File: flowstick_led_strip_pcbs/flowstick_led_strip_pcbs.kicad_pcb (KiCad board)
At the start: 2 copper layers, 8.6 x 127.4 mm, 92 parts, among them J1 LED, J2 LED

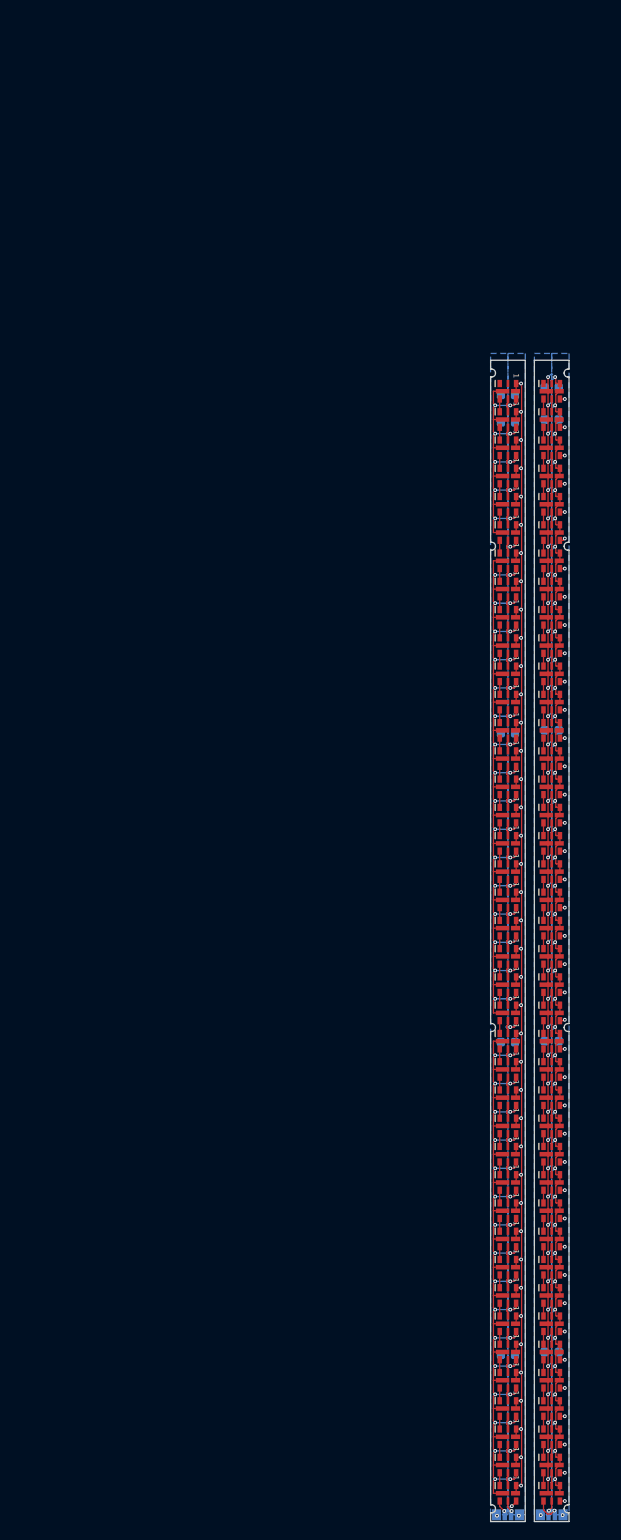
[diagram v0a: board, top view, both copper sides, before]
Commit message: work on rev2 + panelize LED strips
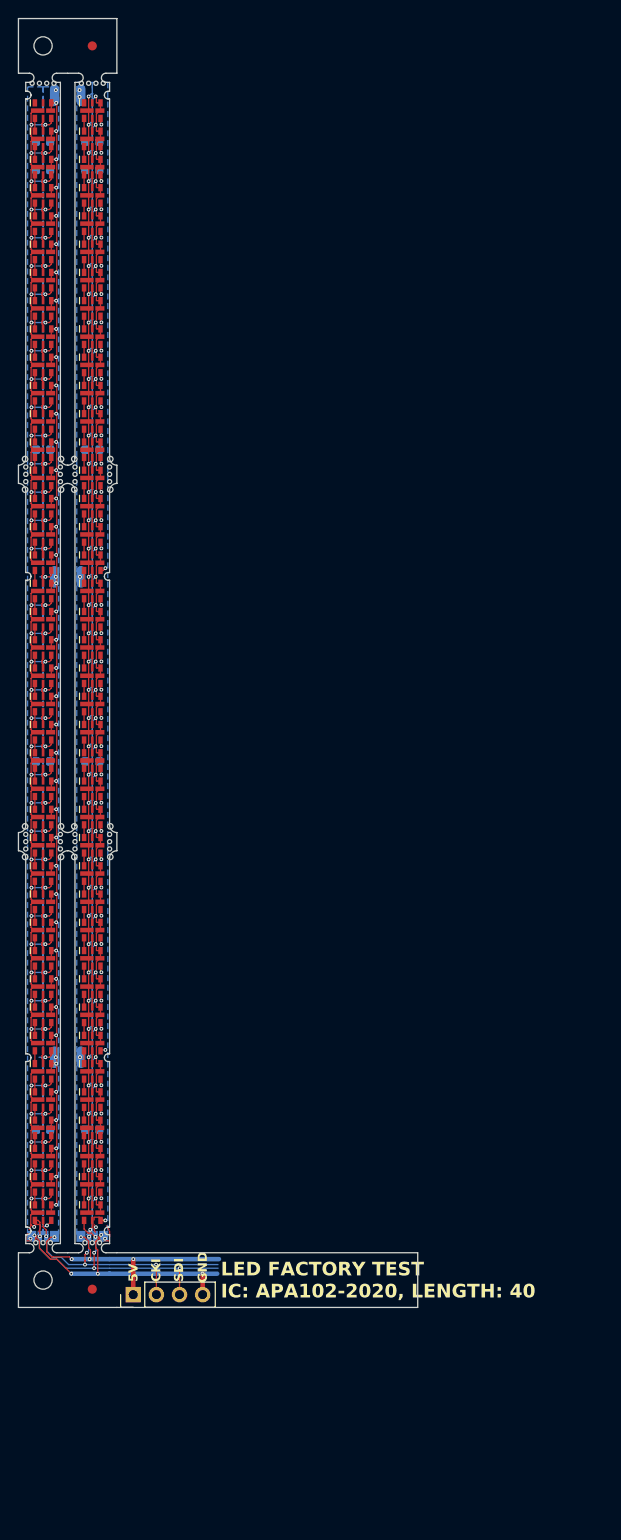
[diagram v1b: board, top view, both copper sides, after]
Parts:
- added H1: MountingHole_Pad, custom:single_b2b_pad_doublewide, B.Cu at (52.1, 136.5)
- added H2: MountingHole_Pad, custom:single_b2b_pad_doublewide, B.Cu at (55.0, 136.5)
- added H3: MountingHole_Pad, custom:single_b2b_pad_doublewide, B.Cu at (52.1, 83.8)
- added H4: MountingHole_Pad, custom:single_b2b_pad_doublewide, B.Cu at (55.0, 83.8)
- added H5: MountingHole_Pad, custom:single_b2b_pad_doublewide, B.Cu at (52.1, 30.9)
- added H6: MountingHole_Pad, custom:single_b2b_pad_doublewide, B.Cu at (55.0, 30.9)
- added J3: FACTORY_TEST, Connector_PinHeader_2.54mm:PinHeader_1x04_P2.54mm_Vertical, F.Cu at (60.8, 162.5)
- added REF**: mousebite_mini4, custom:mousebite_mini4, F.Cu at (50.9, 29.6)
- added REF**: mousebite_5, custom:mousebite_5, F.Cu at (49.0, 72.5)
- added REF**: Fiducial_1mm_Mask2mm, Fiducial:Fiducial_1mm_Mask2mm, F.Cu at (56.3, 161.9)
- added REF**: mousebite_mini3, custom:mousebite_mini3, F.Cu at (50.9, 156.8)
- added REF**: mousebite_5, custom:mousebite_5, F.Cu at (58.2, 112.8)
- added REF**: MountingHole_2mm, MountingHole:MountingHole_2mm, F.Cu at (50.9, 160.9)
- added REF**: mousebite_5, custom:mousebite_5, F.Cu at (52.8, 112.8)
- added REF**: mousebite_mini4, custom:mousebite_mini4, F.Cu at (56.3, 29.6)
- added REF**: mousebite_5, custom:mousebite_5, F.Cu at (54.4, 112.8)
- added REF**: mousebite_5, custom:mousebite_5, F.Cu at (58.2, 72.5)
- added REF**: mousebite_5, custom:mousebite_5, F.Cu at (54.4, 72.5)
- added REF**: MountingHole_2mm, MountingHole:MountingHole_2mm, F.Cu at (50.9, 25.5)
- added REF**: mousebite_5, custom:mousebite_5, F.Cu at (52.8, 72.5)
- added REF**: mousebite_mini3, custom:mousebite_mini3, F.Cu at (56.3, 156.8)
- added REF**: mousebite_5, custom:mousebite_5, F.Cu at (49.0, 112.8)
- added REF**: Fiducial_1mm_Mask2mm, Fiducial:Fiducial_1mm_Mask2mm, F.Cu at (56.3, 25.5)
- moved C3 59.7 mm to (50.9, 69.8)
- moved D1 59.6 mm to (50.9, 153.5)
- moved D6 59.6 mm to (50.9, 138.0)
- moved C2 59.6 mm to (50.9, 104.0)
- moved D10 59.6 mm to (50.9, 125.6)
- moved D11 59.6 mm to (50.9, 122.5)
- moved D12 59.6 mm to (50.9, 119.4)
- moved D14 59.6 mm to (50.9, 113.2)
- moved D15 59.6 mm to (50.9, 110.1)
- moved D16 59.6 mm to (50.9, 107.0)
- moved D17 59.6 mm to (50.9, 103.9)
- moved D18 59.6 mm to (50.9, 100.8)
- moved D19 59.6 mm to (50.9, 97.7)
- moved D2 59.6 mm to (50.9, 150.4)
- moved D20 59.6 mm to (50.9, 94.6)
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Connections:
- C10 pad 1: /strip_r/+5V -> /strip_l/+5V
- C10 pad 2: /strip_r/GND -> /strip_l/GND
- C6 pad 1: /strip_r/+5V -> /strip_l/+5V
- C6 pad 2: /strip_r/GND -> /strip_l/GND
- C7 pad 1: /strip_r/+5V -> /strip_l/+5V
- C7 pad 2: /strip_r/GND -> /strip_l/GND
- C8 pad 1: /strip_r/+5V -> /strip_l/+5V
- C8 pad 2: /strip_r/GND -> /strip_l/GND
- C9 pad 1: /strip_r/+5V -> /strip_l/+5V
- C9 pad 2: /strip_r/GND -> /strip_l/GND
- D41 pad 1: /strip_r/+5V -> /strip_l/+5V
- D41 pad 4: /strip_r/SDI -> /strip_l/SDI
- D41 pad 5: /strip_r/CKI -> /strip_l/CKI
- D41 pad 6: /strip_r/GND -> /strip_l/GND
- D42 pad 1: /strip_r/+5V -> /strip_l/+5V
- D42 pad 6: /strip_r/GND -> /strip_l/GND
- D43 pad 1: /strip_r/+5V -> /strip_l/+5V
- D43 pad 6: /strip_r/GND -> /strip_l/GND
- D44 pad 1: /strip_r/+5V -> /strip_l/+5V
- D44 pad 6: /strip_r/GND -> /strip_l/GND
- D45 pad 1: /strip_r/+5V -> /strip_l/+5V
- D45 pad 6: /strip_r/GND -> /strip_l/GND
- D46 pad 1: /strip_r/+5V -> /strip_l/+5V
- D46 pad 6: /strip_r/GND -> /strip_l/GND
- D47 pad 1: /strip_r/+5V -> /strip_l/+5V
- D47 pad 6: /strip_r/GND -> /strip_l/GND
- D48 pad 1: /strip_r/+5V -> /strip_l/+5V
- D48 pad 6: /strip_r/GND -> /strip_l/GND
- D49 pad 1: /strip_r/+5V -> /strip_l/+5V
- D49 pad 6: /strip_r/GND -> /strip_l/GND
- D50 pad 1: /strip_r/+5V -> /strip_l/+5V
- D50 pad 6: /strip_r/GND -> /strip_l/GND
- D51 pad 1: /strip_r/+5V -> /strip_l/+5V
- D51 pad 6: /strip_r/GND -> /strip_l/GND
- D52 pad 1: /strip_r/+5V -> /strip_l/+5V
- D52 pad 6: /strip_r/GND -> /strip_l/GND
- D53 pad 1: /strip_r/+5V -> /strip_l/+5V
- D53 pad 6: /strip_r/GND -> /strip_l/GND
- D54 pad 1: /strip_r/+5V -> /strip_l/+5V
- D54 pad 6: /strip_r/GND -> /strip_l/GND
- D55 pad 1: /strip_r/+5V -> /strip_l/+5V
- D55 pad 6: /strip_r/GND -> /strip_l/GND
- D56 pad 1: /strip_r/+5V -> /strip_l/+5V
- D56 pad 6: /strip_r/GND -> /strip_l/GND
- D57 pad 1: /strip_r/+5V -> /strip_l/+5V
- D57 pad 6: /strip_r/GND -> /strip_l/GND
- D58 pad 1: /strip_r/+5V -> /strip_l/+5V
- D58 pad 6: /strip_r/GND -> /strip_l/GND
- D59 pad 1: /strip_r/+5V -> /strip_l/+5V
- D59 pad 6: /strip_r/GND -> /strip_l/GND
- D60 pad 1: /strip_r/+5V -> /strip_l/+5V
- D60 pad 6: /strip_r/GND -> /strip_l/GND
- D61 pad 1: /strip_r/+5V -> /strip_l/+5V
- D61 pad 6: /strip_r/GND -> /strip_l/GND
- D62 pad 1: /strip_r/+5V -> /strip_l/+5V
- D62 pad 6: /strip_r/GND -> /strip_l/GND
- D63 pad 1: /strip_r/+5V -> /strip_l/+5V
- D63 pad 6: /strip_r/GND -> /strip_l/GND
- D64 pad 1: /strip_r/+5V -> /strip_l/+5V
- D64 pad 6: /strip_r/GND -> /strip_l/GND
- D65 pad 1: /strip_r/+5V -> /strip_l/+5V
- D65 pad 6: /strip_r/GND -> /strip_l/GND
- D66 pad 1: /strip_r/+5V -> /strip_l/+5V
- D66 pad 6: /strip_r/GND -> /strip_l/GND
- D67 pad 1: /strip_r/+5V -> /strip_l/+5V
- D67 pad 6: /strip_r/GND -> /strip_l/GND
- D68 pad 1: /strip_r/+5V -> /strip_l/+5V
- D68 pad 6: /strip_r/GND -> /strip_l/GND
- D69 pad 1: /strip_r/+5V -> /strip_l/+5V
- D69 pad 6: /strip_r/GND -> /strip_l/GND
- D70 pad 1: /strip_r/+5V -> /strip_l/+5V
- D70 pad 6: /strip_r/GND -> /strip_l/GND
- D71 pad 1: /strip_r/+5V -> /strip_l/+5V
- D71 pad 6: /strip_r/GND -> /strip_l/GND
- D72 pad 1: /strip_r/+5V -> /strip_l/+5V
- D72 pad 6: /strip_r/GND -> /strip_l/GND
- D73 pad 1: /strip_r/+5V -> /strip_l/+5V
- D73 pad 6: /strip_r/GND -> /strip_l/GND
- D74 pad 1: /strip_r/+5V -> /strip_l/+5V
- D74 pad 6: /strip_r/GND -> /strip_l/GND
- D75 pad 1: /strip_r/+5V -> /strip_l/+5V
- D75 pad 6: /strip_r/GND -> /strip_l/GND
- D76 pad 1: /strip_r/+5V -> /strip_l/+5V
- D76 pad 6: /strip_r/GND -> /strip_l/GND
- D77 pad 1: /strip_r/+5V -> /strip_l/+5V
- D77 pad 6: /strip_r/GND -> /strip_l/GND
- D78 pad 1: /strip_r/+5V -> /strip_l/+5V
- D78 pad 6: /strip_r/GND -> /strip_l/GND
- D79 pad 1: /strip_r/+5V -> /strip_l/+5V
- D79 pad 6: /strip_r/GND -> /strip_l/GND
- D80 pad 1: /strip_r/+5V -> /strip_l/+5V
- D80 pad 6: /strip_r/GND -> /strip_l/GND
- J2 pad 1: /strip_r/+5V -> /strip_l/+5V
- J2 pad 2: /strip_r/CKI -> /strip_l/CKI
- J2 pad 3: /strip_r/SDI -> /strip_l/SDI
- J2 pad 4: /strip_r/GND -> /strip_l/GND
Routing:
- net /strip_l/GND: track 272.2 -> 481.1 mm, vias 78 -> 166
- net /strip_l/+5V: track 179.5 -> 382.3 mm, vias 41 -> 92
- net /strip_r/GND: track 175.8 -> 0.00 mm, vias 81 -> 0
- net /strip_r/+5V: track 174.4 -> 0.00 mm, vias 41 -> 0
- net /strip_l/SDI: track 1.83 -> 33.2 mm, vias 1 -> 5
- net /strip_l/CKI: track 1.79 -> 30.8 mm, vias 1 -> 6
- net /strip_r/SDI: track 3.09 -> 0.00 mm, vias 1 -> 0
- net /strip_r/CKI: track 1.74 -> 0.00 mm, vias 1 -> 0
- added copper zone on F.Cu, net /strip_l/GND
- removed copper zone on B.Cu, net /strip_r/+5V
- removed copper zone on B.Cu, net /strip_r/GND
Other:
- board size 8.6 x 127.4 mm -> 43.8 x 141.4 mm
- board text added: "5V"
- board text added: "CKI"
- board text added: "GND"
- board text added: "L"
- board text added: "LED FACTORY TEST IC: APA102-2020, LENGTH: 40"
- board text added: "R"
- board text added: "SDI"
- board text added: "rev 2"

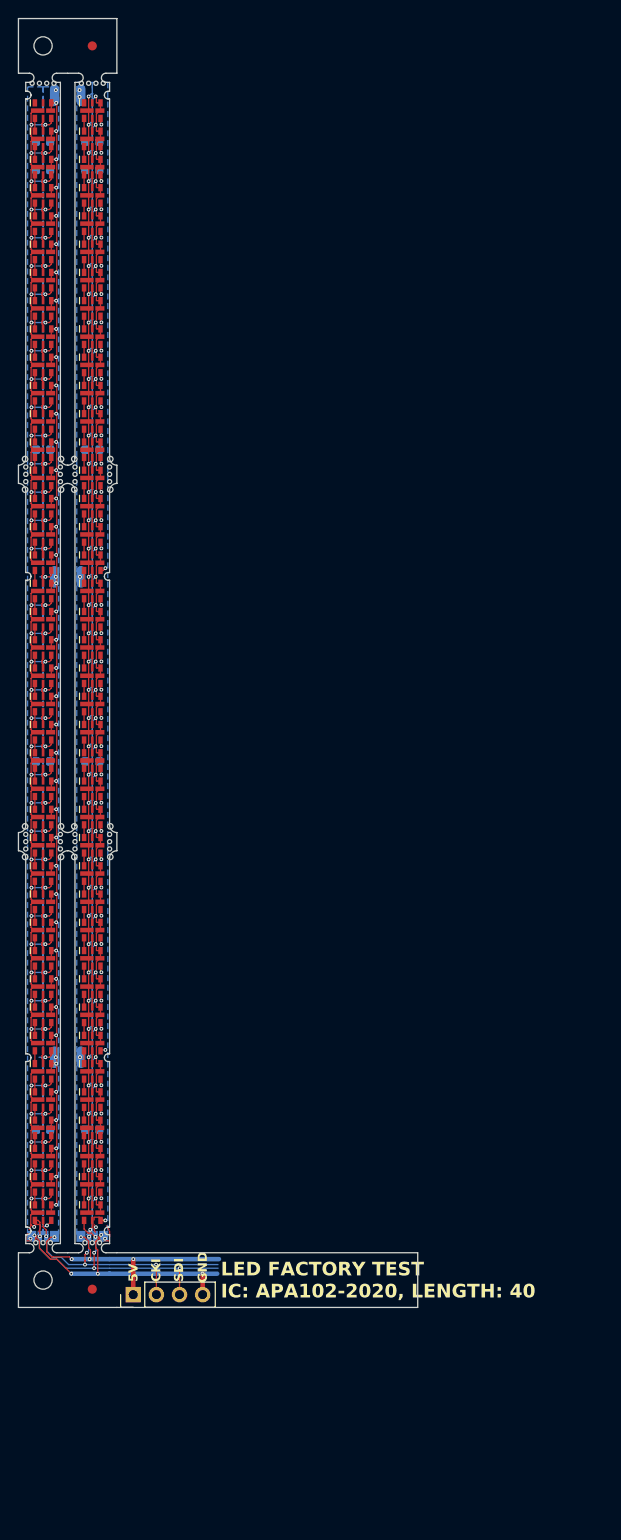
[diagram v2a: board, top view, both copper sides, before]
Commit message: Update LED strips to use to 6-pin LED package
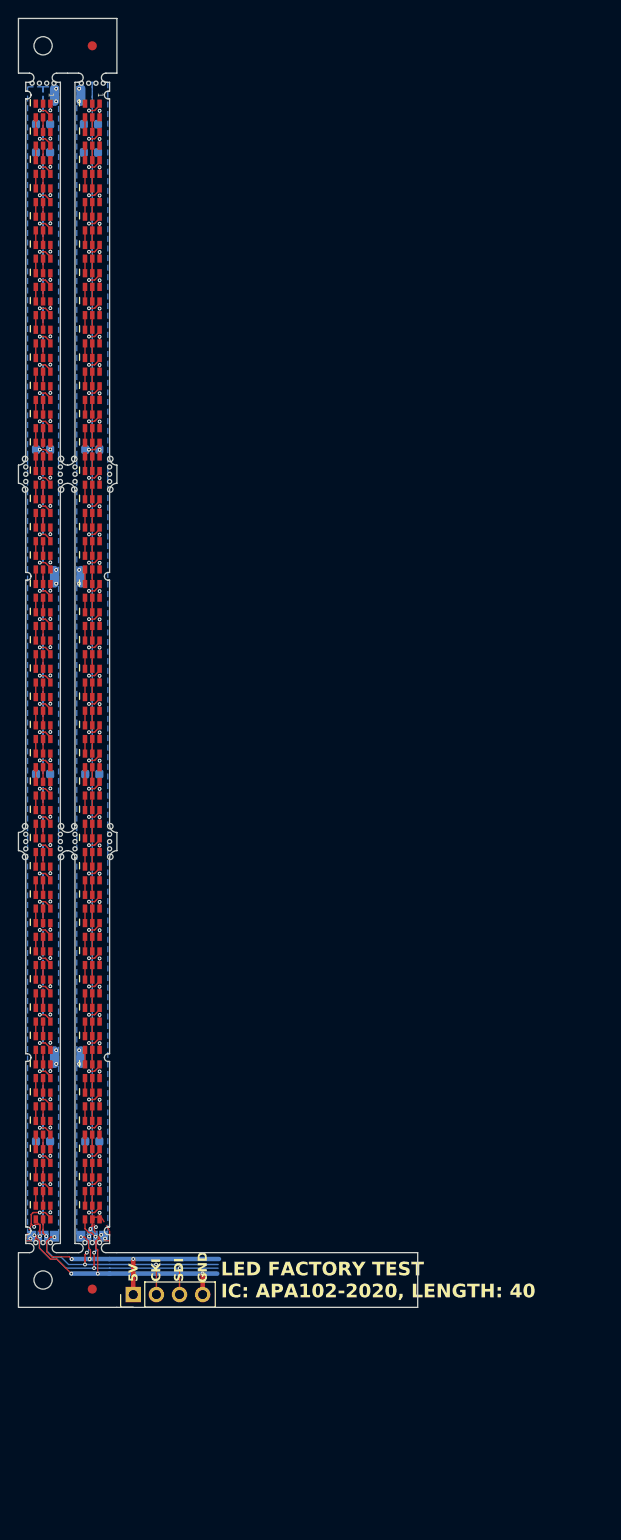
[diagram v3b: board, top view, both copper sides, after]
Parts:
- D1, D10, D11, D12, D13, D14, D15, D16, D17, D18, D19, D2, D20, D21, D22, D23, D24, D25, D26, D27, D28, D29, D3, D30, D31, D32, D33, D34, D35, D36, D37, D38, D39, D4, D40, D41, D42, D43, D44, D45, D46, D47, D48, D49, D5, D50, D51, D52, D53, D54, D55, D56, D57, D58, D59, D6, D60, D61, D62, D63, D64, D65, D66, D67, D68, D69, D7, D70, D71, D72, D73, D74, D75, D76, D77, D78, D79, D8, D80, D9: footprint LED_SMD:LED-APA102-2020 -> custom:LED-APA102-2020-6
- moved C10 1.92 mm to (56.1, 34.1)
- moved C9 1.92 mm to (56.1, 37.2)
- moved C4 1.91 mm to (50.9, 37.2)
- moved C5 1.91 mm to (50.9, 34.1)
- moved C2 1.39 mm to (50.9, 105.4)
- moved C7 1.39 mm to (56.3, 105.4)
- moved C1 1.29 mm to (50.9, 145.7)
- moved C6 1.29 mm to (56.3, 145.7)
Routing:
- net /strip_l/GND: track 481.1 -> 124.5 mm, vias 166 -> 89
- net /strip_l/+5V: track 382.3 -> 131.0 mm, vias 92 -> 97
- net /strip_l/CKI: track 30.8 -> 32.6 mm

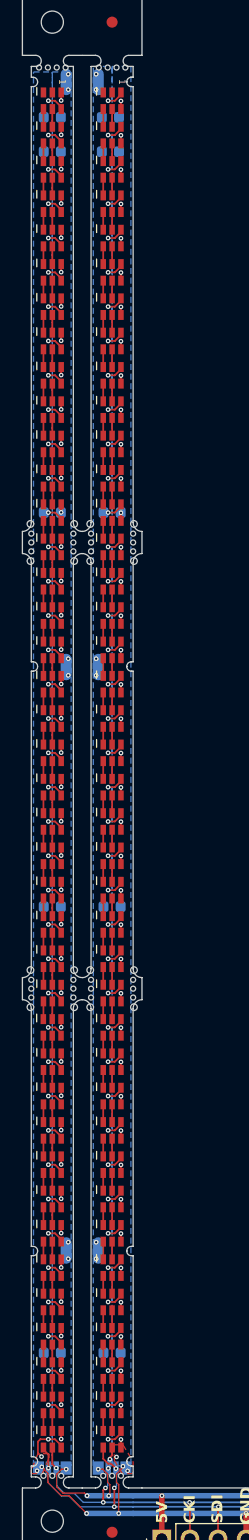
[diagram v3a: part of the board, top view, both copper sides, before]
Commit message: Switch to 90 degree alternate LED pinout
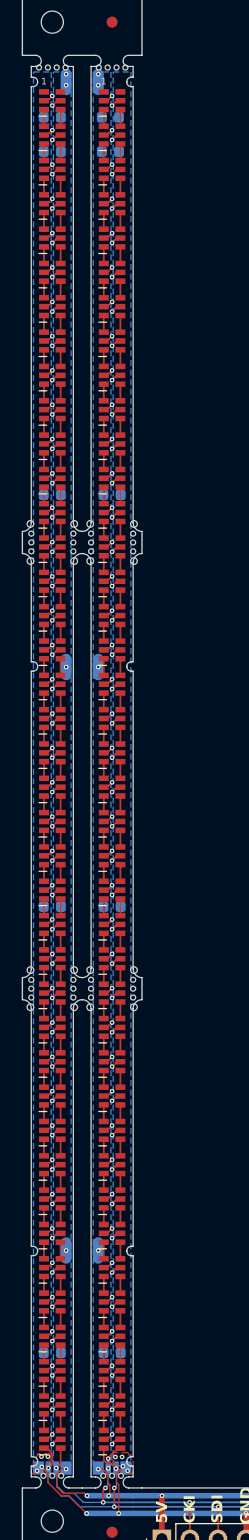
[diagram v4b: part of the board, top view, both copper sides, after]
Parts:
- D1, D10, D11, D12, D13, D14, D15, D16, D17, D18, D19, D2, D20, D21, D22, D23, D24, D25, D26, D27, D28, D29, D3, D30, D31, D32, D33, D34, D35, D36, D37, D38, D39, D4, D40, D41, D42, D43, D44, D45, D46, D47, D48, D49, D5, D50, D51, D52, D53, D54, D55, D56, D57, D58, D59, D6, D60, D61, D62, D63, D64, D65, D66, D67, D68, D69, D7, D70, D71, D72, D73, D74, D75, D76, D77, D78, D79, D8, D80, D9: footprint custom:LED-APA102-2020-6 -> custom:LED-APA102-2020-6_90deg
- moved C3 1.60 mm to (50.9, 68.2)
- moved C8 1.60 mm to (56.3, 68.2)
- turned D13 to 0 degrees
- turned D42 to 0 degrees
- turned D44 to 0 degrees
- turned D1 to 0 degrees
- turned D10 to 0 degrees
- turned D11 to 0 degrees
- turned D12 to 0 degrees
- turned D14 to 0 degrees
- turned D15 to 0 degrees
- turned D16 to 0 degrees
- turned D17 to 0 degrees
- turned D18 to 0 degrees
- turned D19 to 0 degrees
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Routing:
- net /strip_l/GND: track 124.5 -> 103.7 mm, vias 89 -> 91
- net /strip_l/+5V: track 131.0 -> 112.8 mm, vias 97 -> 93
- net /strip_l/CKI: track 32.6 -> 32.1 mm
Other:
- board text added: "rev 2 alt LED"
- board text removed: "rev 2"
